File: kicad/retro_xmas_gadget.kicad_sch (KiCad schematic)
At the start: 77 parts, among them J1 USB_C_Receptacle_USB2.0_16P, J2 SD_Card_Receptacle, J3 AudioJack3_SwitchTR, J4 Conn_01x18, J5 Conn_01x02, J6 Conn_01x03, J7 Conn_01x03, J8 Conn_01x07, Q1 UMH3N, Q2 SS8050, SW1 RESET, SW10 SELECT, SW11 START, SW12 A, SW13 B, SW2 BOOT, SW3 KH-SS12F23-G6, SW4 UP, SW5 DOWN, SW6 LEFT, SW7 RIGHT, SW8 MENU, SW9 OPTION, U1 CP2102N-Axx-xQFN28, U2 ESP32-S3-WROOM-1, U4 XC6210B332MR, U5 TP4056

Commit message: run down checking points
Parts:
- added C17: 100nf, Capacitor_SMD:C_0603_1608Metric_Pad1.08x0.95mm_HandSolder, symbol Device:C
- added R17: 15k, Resistor_SMD:R_0603_1608Metric_Pad0.98x0.95mm_HandSolder, symbol Device:R
- added R23: 5.1k, Resistor_SMD:R_0603_1608Metric_Pad0.98x0.95mm_HandSolder, symbol Device:R
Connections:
- net GND: now also U3.9 (EP), U5.9 (EP), C17.1, R23.1; no longer J2.13 (SHELL2)
- net VBUS: now also R17.2
- net at U5.1 (TEMP): now also C17.2, R17.1, R23.2
- no-connect marks 35 -> 33
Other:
- note added: "SD Card Pins"
- note added: "Switch Position and Model"
- note removed: "Battery thermal sensor"
- note removed: "Check where EP's should be connected"
- moved on the sheet: C14, D3, D4, R14, R15, R16, U5

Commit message: final improvements and checks
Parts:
- H7: footprint MountingHole:MountingHole_4.3mm_M4 -> MountingHole:MountingHole_3.5mm
- J5: footprint Connector_JST:JST_SH_SM02B-SRSS-TB_1x02-1MP_P1.00mm_Horizontal -> AMPHENOL_10114830-10102LF:AMPHENOL_10114830-10102LF
- J6: footprint Connector_JST:JST_GH_SM03B-GHS-TB_1x03-1MP_P1.25mm_Horizontal -> AMPHENOL_10114830-10103LF:AMPHENOL_10114830-10103LF
- L1: footprint Inductor_SMD:L_0603_1608Metric_Pad1.05x0.95mm_HandSolder -> Inductor_SMD:L_0805_2012Metric_Pad1.05x1.20mm_HandSolder
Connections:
- net AUDIO-: now also J5.1 (Pin_1); no longer J5.2 (Pin_2)
- net SPK+: now also J5.2 (Pin_2); no longer J5.1 (Pin_1)
- net Temp: now reaches J6.2 (Pin_2)
- net Temp: now also C17.2, R17.1, R23.2, U5.1 (TEMP)
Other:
- note added: "Check L1, make 0805?"
- note removed: "Controlled impedance for USB D- and D+?"
- note removed: "Mounting hole sizes"
- note removed: "SD Card Pins"
- note removed: "Switch Position and Model"
- note removed: "capacitor, which sizes?"
- moved on the sheet: C17, R23

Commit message: improvements and corrections
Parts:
- D1: value BAT54J -> CRS08; footprint Diode_SMD:D_SOD-323_HandSoldering -> Diode_SMD:D_SOD-123
- R17: now not fitted
- R23: value 5.1k -> 0R; now fitted
- U3, U5: footprint Package_SO:SOP-8-1EP_4.57x4.57mm_P1.27mm_EP4.57x4.45mm_ThermalVias -> Package_SO:SOIC-8-1EP_3.9x4.9mm_P1.27mm_EP2.41x3.3mm_ThermalVias
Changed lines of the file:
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@@
 			)
 		)
-		(property "Footprint" "Package_SO:SOP-8-1EP_4.57x4.57mm_P1.27mm_EP4.57x4.45mm_ThermalVias"
+		(property "Footprint" "Package_SO:SOIC-8-1EP_3.9x4.9mm_P1.27mm_EP2.41x3.3mm_ThermalVias"
 			(at 119.38 153.67 0)
 			(effects
@@
 		(in_bom yes)
 		(on_board yes)
-		(dnp no)
+		(dnp yes)
 		(property "Reference" "R17"
 			(at 27.94 123.19 0)
@@
 			)
 		)
-		(property "Footprint" "Package_SO:SOP-8-1EP_4.57x4.57mm_P1.27mm_EP4.57x4.45mm_ThermalVias"
+		(property "Footprint" "Package_SO:SOIC-8-1EP_3.9x4.9mm_P1.27mm_EP2.41x3.3mm_ThermalVias"
 			(at 46.99 133.35 0)
 			(effects
@@
 			)
 		)
-		(property "Value" "BAT54J"
+		(property "Value" "CRS08"
 			(at 56.1975 29.21 0)
 			(effects
@@
 			)
 		)
-		(property "Footprint" "Diode_SMD:D_SOD-323_HandSoldering"
+		(property "Footprint" "Diode_SMD:D_SOD-123"
 			(at 55.88 33.02 0)
 			(effects
@@
 		(in_bom yes)
 		(on_board yes)
-		(dnp yes)
+		(dnp no)
 		(property "Reference" "R23"
 			(at 24.13 145.034 0)
@@
 			)
 		)
-		(property "Value" "5.1k"
+		(property "Value" "0R"
 			(at 24.13 147.574 0)
 			(effects

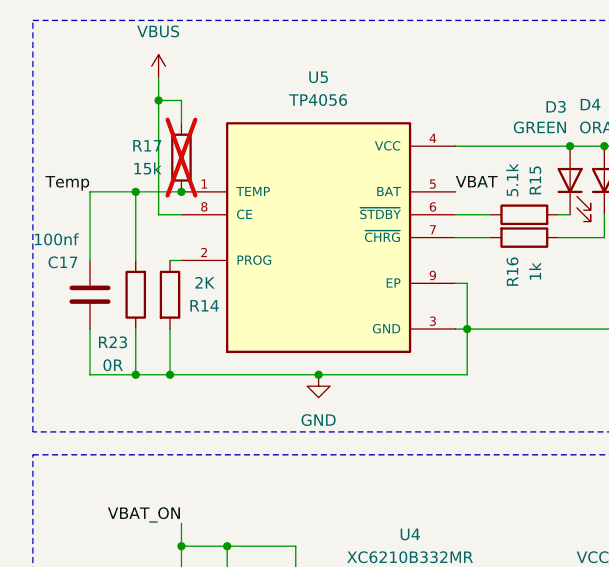
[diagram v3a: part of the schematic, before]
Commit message: update charging resistor
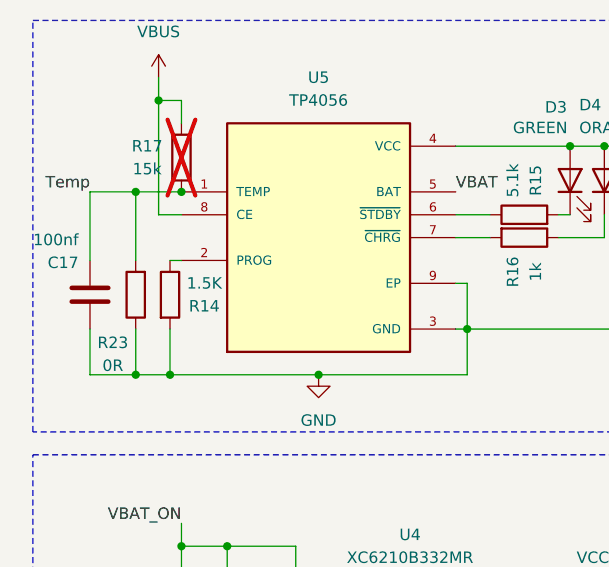
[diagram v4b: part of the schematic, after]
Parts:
- R14: value 2K -> 1.5K
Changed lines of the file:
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@@
 			)
 		)
-		(property "Value" "2K"
+		(property "Value" "1.5K"
 			(at 34.29 138.43 0)
 			(effects

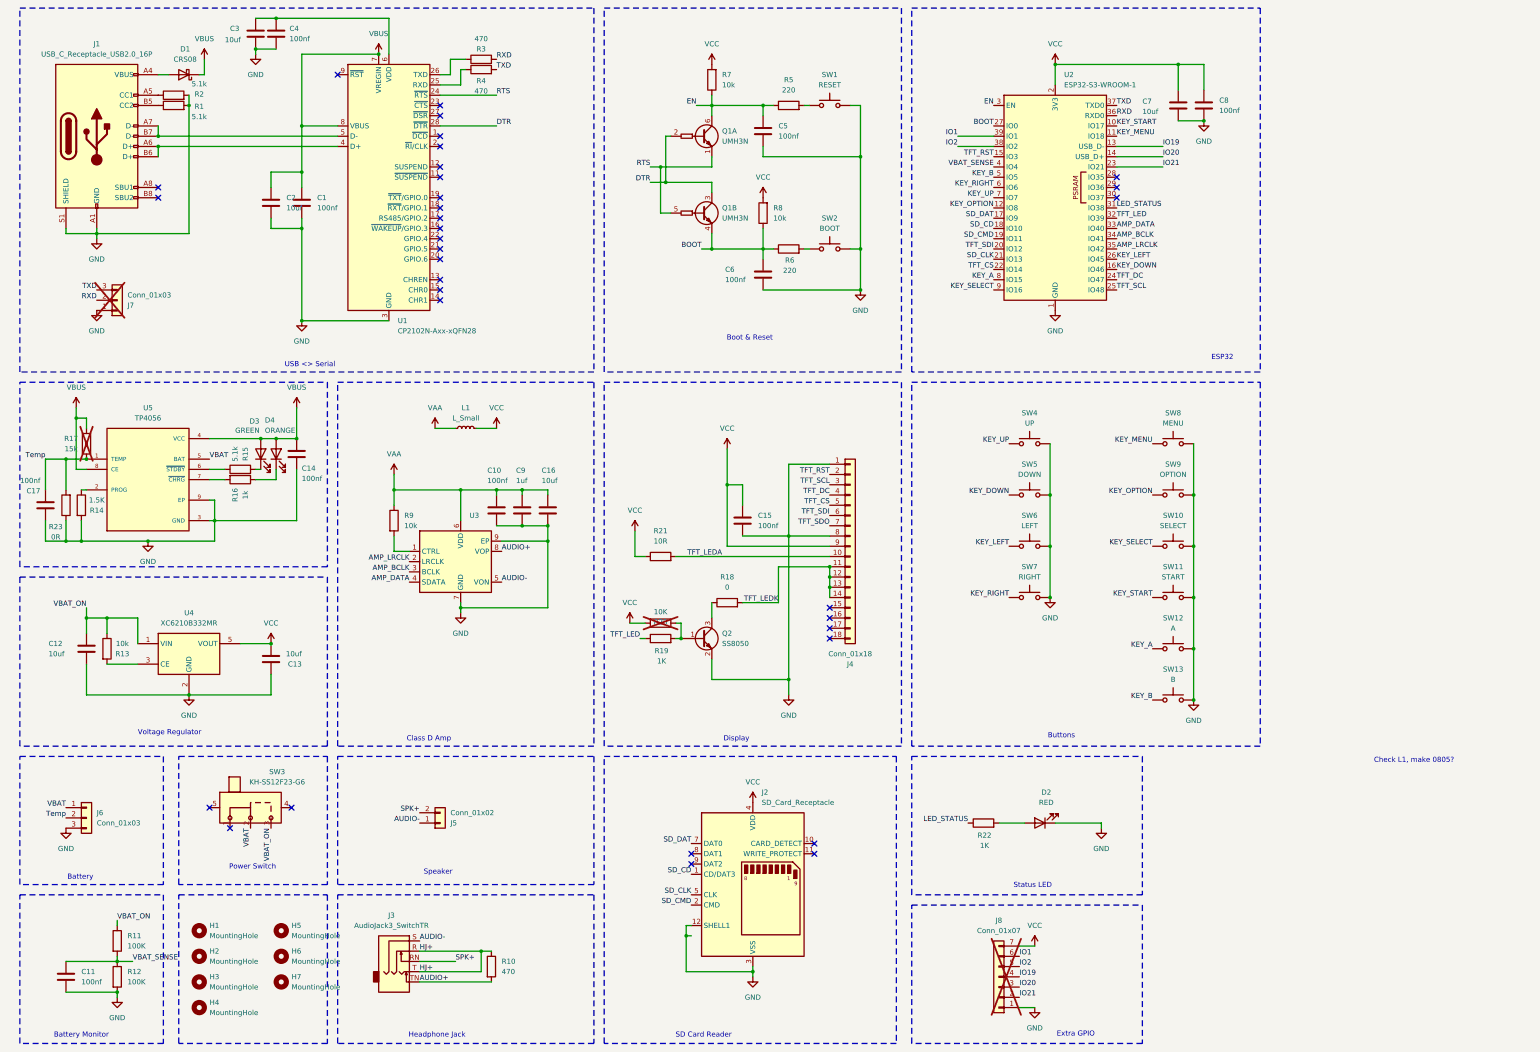
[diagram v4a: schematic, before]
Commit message: load sharing
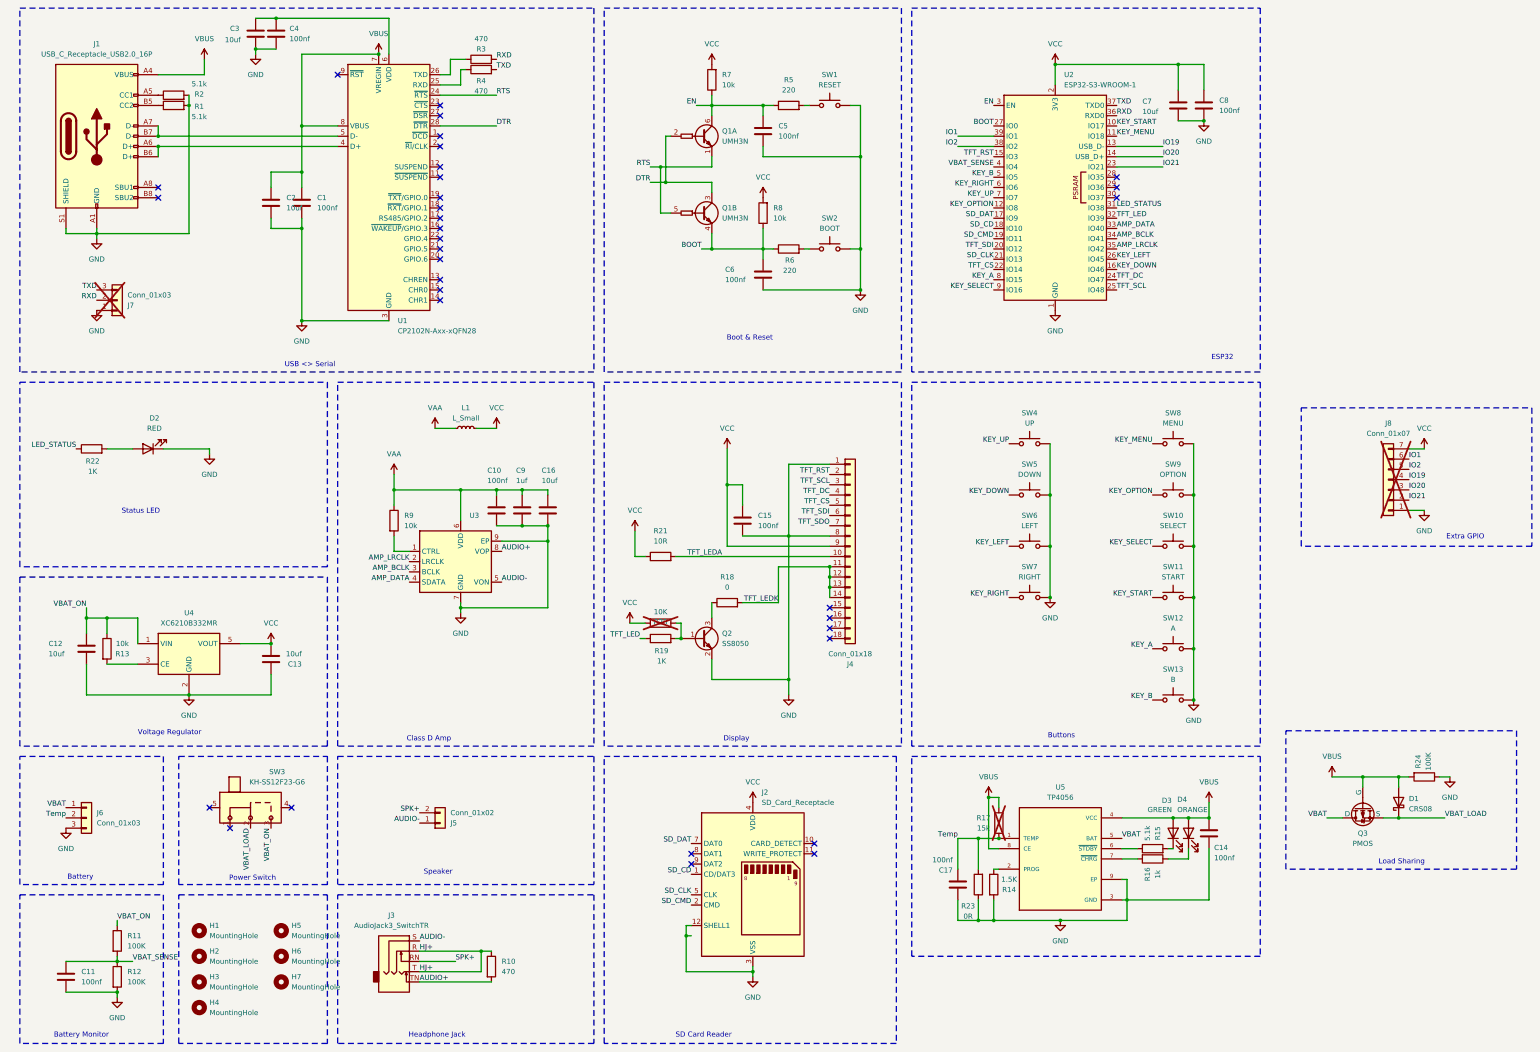
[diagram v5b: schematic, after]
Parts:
- added Q3: PMOS, Package_TO_SOT_SMD:SOT-23_Handsoldering, symbol Simulation_SPICE:PMOS
- added R24: 100K, Resistor_SMD:R_0603_1608Metric_Pad0.98x0.95mm_HandSolder, symbol Device:R
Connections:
- net GND: now also R24.1
- net VBAT: now also Q3.1 (D); no longer SW3.2 (B)
- net VBUS: now also D1.2 (A), J1.A4 (VBUS), J1.A9 (VBUS), J1.B4 (VBUS), J1.B9 (VBUS), Q3.2 (G), R24.2; no longer D1.1 (K)
- new net VBAT_LOAD: D1.1 (K), Q3.3 (S), SW3.2 (B)
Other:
- note added: "Load Sharing"
- note removed: "Check L1, make 0805?"
- moved on the sheet: C14, C17, D1, D2, D3, D4, J8, R14, R15, R16, R17, R22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

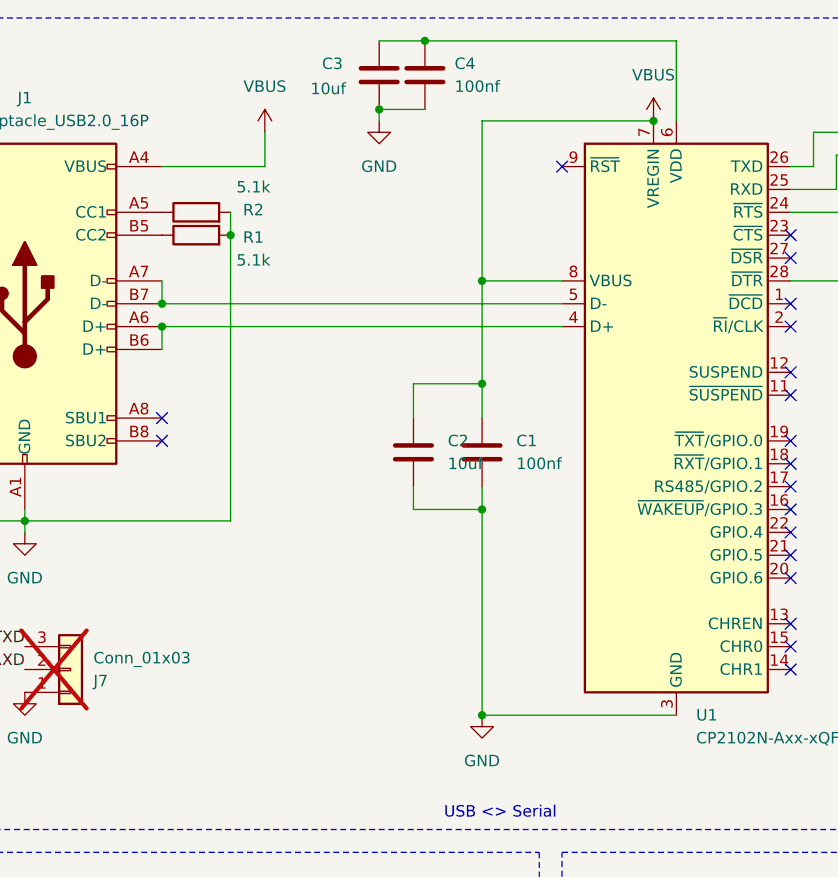
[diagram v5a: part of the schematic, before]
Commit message: add pull up resistor to cp2102 rst
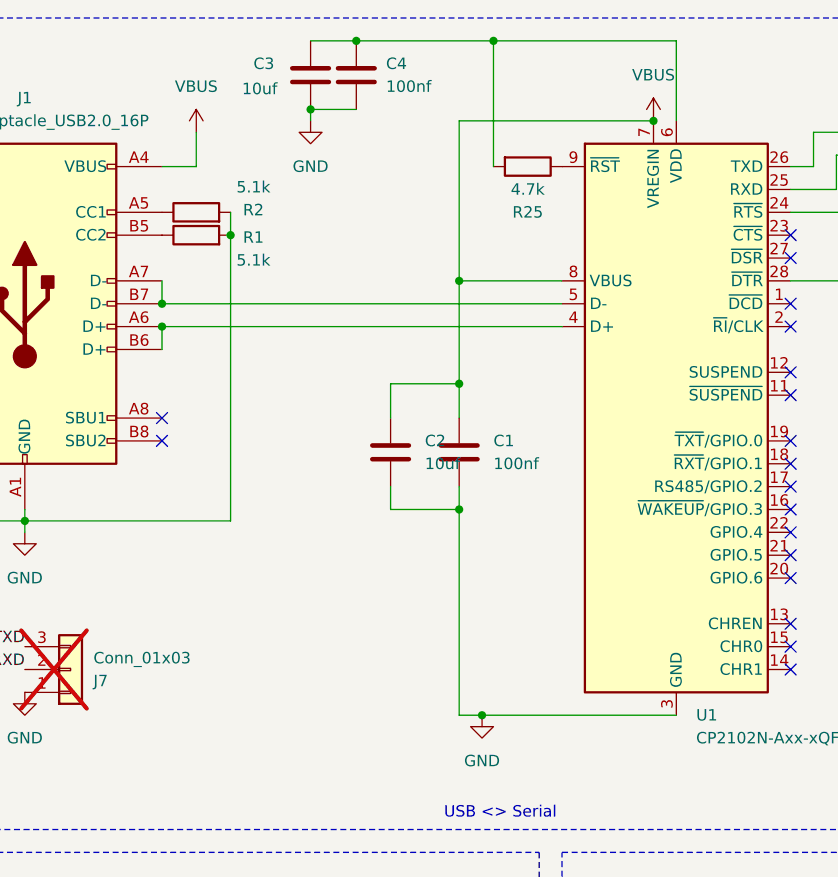
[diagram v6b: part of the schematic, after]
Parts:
- added R25: 4.7k, Resistor_SMD:R_0603_1608Metric_Pad0.98x0.95mm_HandSolder, symbol Device:R
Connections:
- net at C3.1, C4.1, U1.6 (VDD): now also R25.2
- net at U1.9 (~{RST}): now also R25.1
- no-connect marks 33 -> 32
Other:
- moved on the sheet: C1, C2, C3, C4
